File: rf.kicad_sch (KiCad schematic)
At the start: 3 parts, among them J1 ANT_A, J2 ANT_B

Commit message: more stuff
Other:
- moved on the sheet: J1, J2
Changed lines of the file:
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@@
 	)
 	(no_connect
-		(at 196.85 93.98)
+		(at 180.34 93.98)
 	)
 	(wire
 		(pts
-			(xy 175.26 85.09) (xy 196.85 85.09)
+			(xy 175.26 85.09) (xy 180.34 85.09)
 		)
 		(stroke
@@
 		)
 	)
+	(hierarchical_label "TX"
+		(shape output)
+		(at 101.6 95.25 180)
+		(fields_autoplaced yes)
+		(effects
+			(font
+				(size 1.27 1.27)
+			)
+			(justify right)
+		)
+	)
+	(hierarchical_label "DEMOD_OUT"
+		(shape output)
+		(at 101.6 111.76 180)
+		(fields_autoplaced yes)
+		(effects
+			(font
+				(size 1.27 1.27)
+			)
+			(justify right)
+		)
+	)
+	(hierarchical_label "U_BATT"
+		(shape input)
+		(at 101.6 85.09 180)
+		(fields_autoplaced yes)
+		(effects
+			(font
+				(size 1.27 1.27)
+			)
+			(justify right)
+		)
+	)
+	(hierarchical_label "PWR_SEL"
+		(shape input)
+		(at 101.6 102.87 180)
+		(fields_autoplaced yes)
+		(effects
+			(font
+				(size 1.27 1.27)
+			)
+			(justify right)
+		)
+	)
+	(hierarchical_label "ENA"
+		(shape input)
+		(at 101.6 120.65 180)
+		(fields_autoplaced yes)
+		(effects
+			(font
+				(size 1.27 1.27)
+			)
+			(justify right)
+		)
+	)
+	(hierarchical_label "MOD_IN"
+		(shape input)
+		(at 101.6 109.22 180)
+		(fields_autoplaced yes)
+		(effects
+			(font
+				(size 1.27 1.27)
+			)
+			(justify right)
+		)
+	)
+	(hierarchical_label "PTT"
+		(shape input)
+		(at 101.6 116.84 180)
+		(fields_autoplaced yes)
+		(effects
+			(font
+				(size 1.27 1.27)
+			)
+			(justify right)
+		)
+	)
+	(hierarchical_label "RX"
+		(shape input)
+		(at 101.6 97.79 180)
+		(fields_autoplaced yes)
+		(effects
+			(font
+				(size 1.27 1.27)
+			)
+			(justify right)
+		)
+	)
 	(symbol
 		(lib_id "Connector:Conn_01x01_Pin")
-		(at 201.93 85.09 180)
+		(at 185.42 85.09 180)
 		(unit 1)
 		(exclude_from_sim no)
@@
 		(fields_autoplaced yes)
 		(property "Reference" "J1"
-			(at 201.295 80.01 0)
+			(at 184.785 80.01 0)
 			(effects
 				(font
@@
 		)
 		(property "Value" "ANT_A"
-			(at 201.295 82.55 0)
+			(at 184.785 82.55 0)
 			(effects
 				(font
@@
 		)
 		(property "Footprint" "TestPoint:TestPoint_Pad_D2.5mm"
-			(at 201.93 85.09 0)
+			(at 185.42 85.09 0)
 			(effects
 				(font
@@
 		)
 		(property "Datasheet" "~"
-			(at 201.93 85.09 0)
+			(at 185.42 85.09 0)
 			(effects
 				(font
@@
 		)
 		(property "Description" "Generic connector, single row, 01x01, script generated"
-			(at 201.93 85.09 0)
+			(at 185.42 85.09 0)
 			(effects
 				(font
@@
 	(symbol
 		(lib_id "Connector:Conn_01x01_Pin")
-		(at 201.93 93.98 180)
+		(at 185.42 93.98 180)
 		(unit 1)
 		(exclude_from_sim no)
@@
 		(fields_autoplaced yes)
 		(property "Reference" "J2"
-			(at 201.295 88.9 0)
+			(at 184.785 88.9 0)
 			(effects
 				(font
@@
 		)
 		(property "Value" "ANT_B"
-			(at 201.295 91.44 0)
+			(at 184.785 91.44 0)
 			(effects
 				(font
@@
 		)
 		(property "Footprint" "TestPoint:TestPoint_Pad_D2.5mm"
-			(at 201.93 93.98 0)
+			(at 185.42 93.98 0)
 			(effects
 				(font
@@
 		)
 		(property "Datasheet" "~"
-			(at 201.93 93.98 0)
+			(at 185.42 93.98 0)
 			(effects
 				(font
@@
 		)
 		(property "Description" "Generic connector, single row, 01x01, script generated"
-			(at 201.93 93.98 0)
-			(effects
-				(font
+			(at 185.42 93.98 0)
+			(effects
+				(font

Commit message: imported SA868 - thanks, edgetriggered
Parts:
- added U2: SA868, Parts:SA868-VER1.1, symbol Parts:SA868
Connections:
- net DEMOD_OUT: now also U2.3 (AF_OUT)
- net ENA: now also U2.6 (PD)
- net MOD_IN: now also U2.18 (MIC_IN)
- net PTT: now also U2.5 (PTT)
- net PWR_SEL: now also U2.7 (H/L)
- net RX: now also U2.16 (RXD)
- net TX: now also U2.17 (TXD)
- net U_BATT: now also U2.8 (V_{BAT})
- net at FL1.1 (IN): now also U2.12 (ANT)
- net GND: now reaches FL1.2 (GND), FL1.4 (GND)
- net GND: now also U2.10 (GND), U2.9 (GND)
- no-connect marks 1 -> 6
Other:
- note added: "Module programming interface"
- moved on the sheet: FL1, J1, J2

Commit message: connections
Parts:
- renumbered J1 to J2, J2 to J3
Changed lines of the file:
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@@
 	(title_block
 		(title "Mainboard replacement for Nokia 3310")
-		(date "24-10-2024")
+		(date "25-10-2024")
 		(rev "Rev A")
 		(company "M17 Project")
@@
 		(dnp no)
 		(fields_autoplaced yes)
-		(property "Reference" "J1"
+		(property "Reference" "J2"
 			(at 184.785 87.63 0)
 			(effects
@@
 			(project ""
 				(path "/8d65c5ef-7a02-4454-aee5-ab9c49e4aeab/3b860798-5455-4385-a0e7-f7fc9f6a9c55"
-					(reference "J1")
+					(reference "J2")
 					(unit 1)
 				)
@@
 		(dnp no)
 		(fields_autoplaced yes)
-		(property "Reference" "#PWR018"
+		(property "Reference" "#PWR022"
 			(at 165.1 109.22 0)
 			(effects
@@
 			(project ""
 				(path "/8d65c5ef-7a02-4454-aee5-ab9c49e4aeab/3b860798-5455-4385-a0e7-f7fc9f6a9c55"
-					(reference "#PWR018")
+					(reference "#PWR022")
 					(unit 1)
 				)
@@
 		(dnp no)
 		(fields_autoplaced yes)
-		(property "Reference" "J2"
+		(property "Reference" "J3"
 			(at 184.785 96.52 0)
 			(effects
@@
 			(project "M17_3310"
 				(path "/8d65c5ef-7a02-4454-aee5-ab9c49e4aeab/3b860798-5455-4385-a0e7-f7fc9f6a9c55"
-					(reference "J2")
+					(reference "J3")
 					(unit 1)
 				)
@@
 		(dnp no)
 		(fields_autoplaced yes)
-		(property "Reference" "#PWR017"
+		(property "Reference" "#PWR021"
 			(at 121.92 116.84 0)
 			(effects
@@
 			(project "M17_3310"
 				(path "/8d65c5ef-7a02-4454-aee5-ab9c49e4aeab/3b860798-5455-4385-a0e7-f7fc9f6a9c55"
-					(reference "#PWR017")
+					(reference "#PWR021")
 					(unit 1)
 				)

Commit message: audio part
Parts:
- added Q1, Q2: BSS138, Package_TO_SOT_SMD:SOT-23, symbol Transistor_FET:BSS138
- added R7, R8: 100k, Inductor_SMD:L_0805_2012Metric, symbol Device:R
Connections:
- net GND: now also Q1.2 (S), Q2.2 (S), R7.1, R8.1
- net PWR_SEL: now also Q2.1 (G), R8.2; no longer U2.7 (H/L)
- net ENA: no longer names the net of U2.6 (PD)
- net ENA: now also Q1.3 (D)
- new net: Q2.3 (D), U2.7 (H/L)
- new net ~{ENA}: Q1.1 (G), R7.2
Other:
- moved on the sheet: FL1, J2, J3, U2

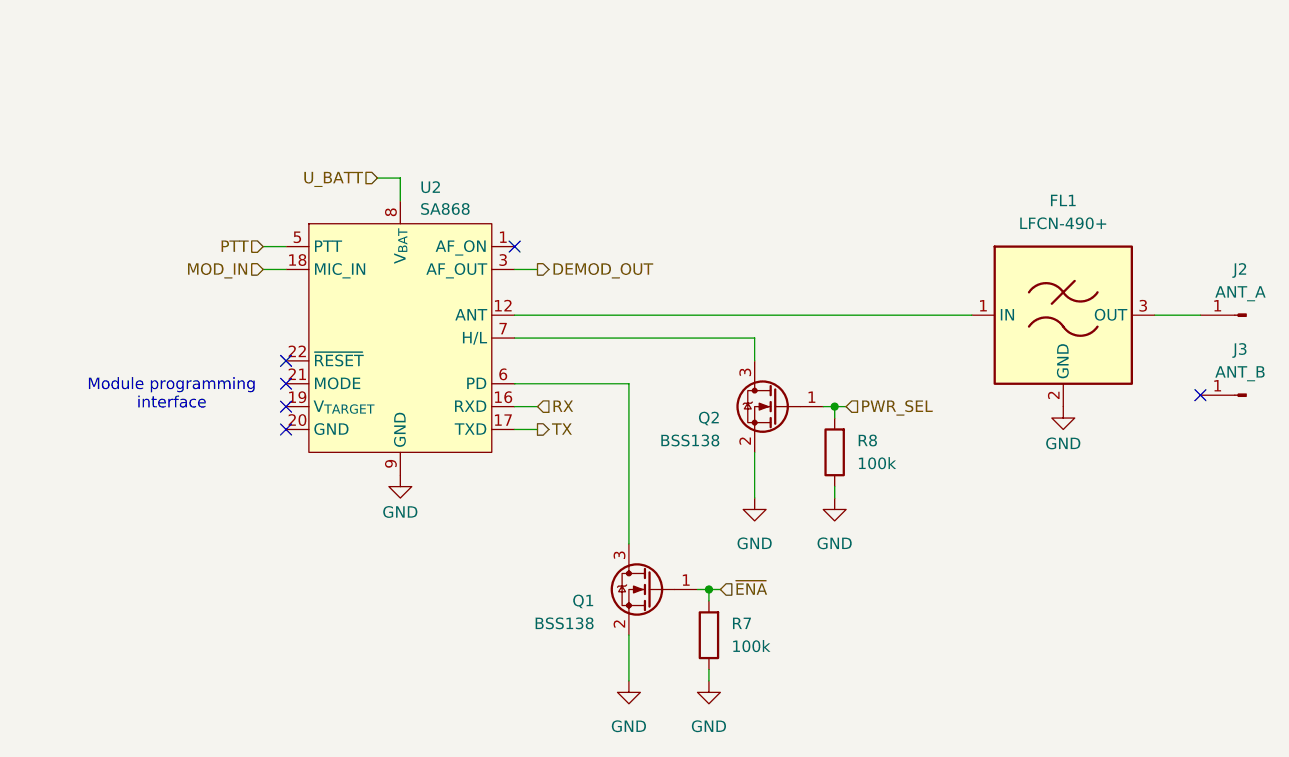
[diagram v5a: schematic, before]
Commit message: spk/mic update
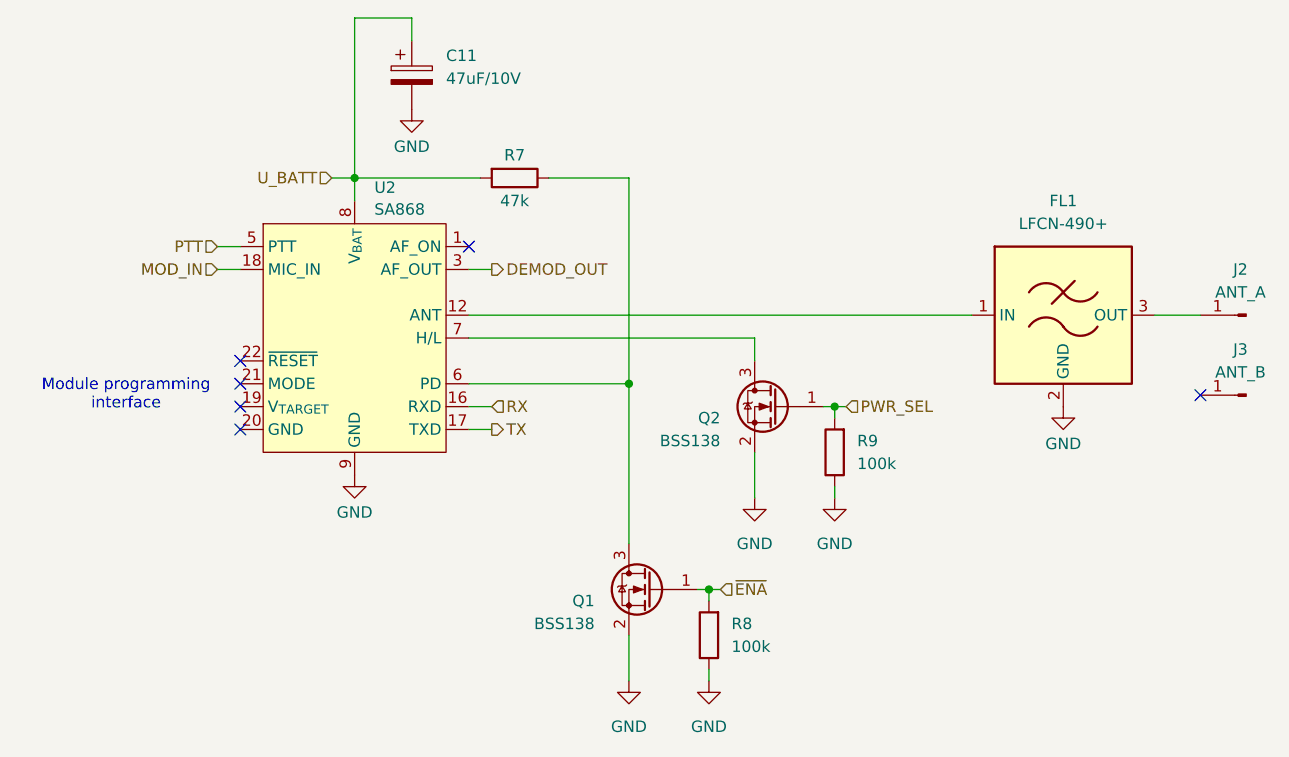
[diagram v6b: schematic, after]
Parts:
- added C11: 47uF/10V, Capacitor_Tantalum_SMD:CP_EIA-3528-21_Kemet-B, symbol Device:C_Polarized
- added R7: 47k, Inductor_SMD:L_0805_2012Metric, symbol Device:R
- renumbered R7 to R8, R8 to R9
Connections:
- net GND: now also C11.2
- net U_BATT: now also C11.1, R7.2
- net at Q1.3 (D), U2.6 (PD): now also R7.1
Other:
- moved on the sheet: U2

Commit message: removed audio part
- added buzzer
- added battery voltage measurement
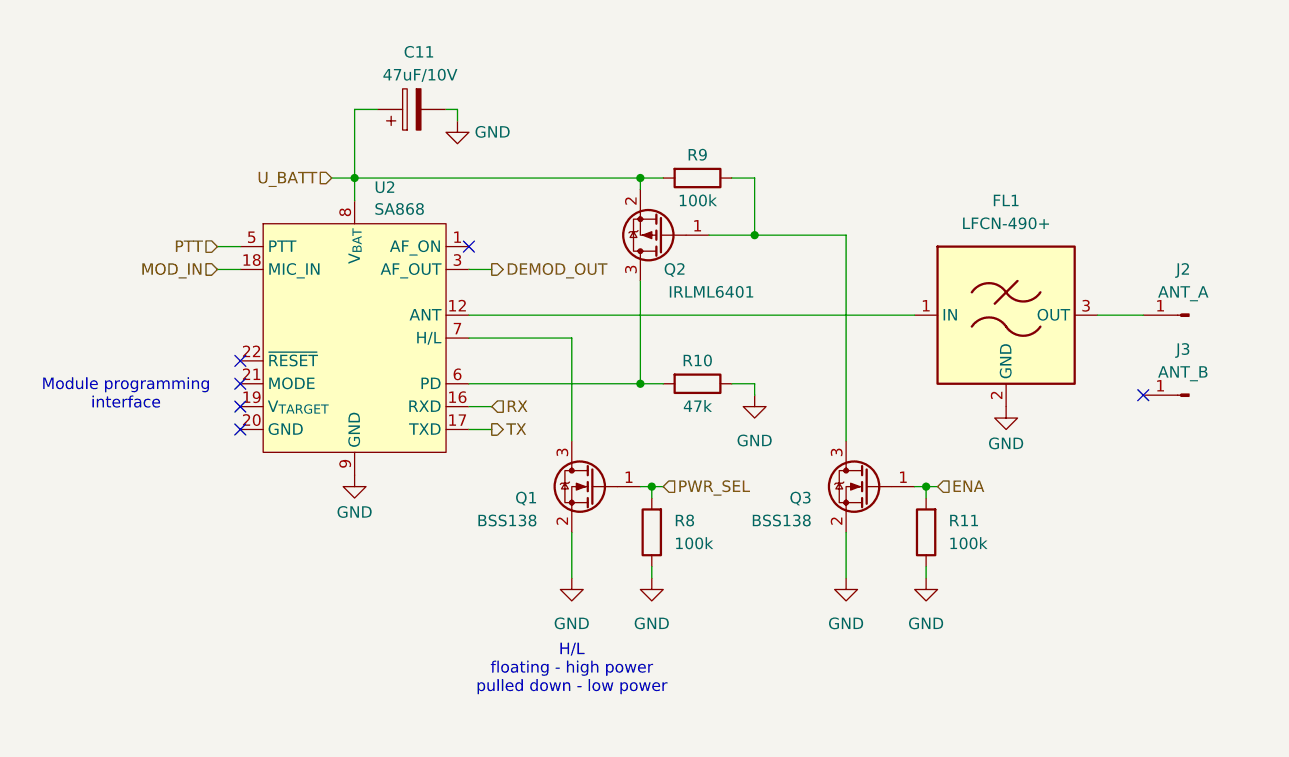
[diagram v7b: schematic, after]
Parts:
- added Q2: IRLML6401, Package_TO_SOT_SMD:SOT-23, symbol Transistor_FET:IRLML6401
- added R10: 47k, Inductor_SMD:L_0805_2012Metric, symbol Device:R
- R9: renamed from R7; value 47k -> 100k
- renumbered Q2 to Q1, Q1 to Q3, R8 to R11, R9 to R8
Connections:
- net GND: now also R10.1
- net U_BATT: now also Q2.2 (S)
- net at Q3.3 (D), R9.1: now also Q2.1 (G); no longer U2.6 (PD)
- net ~{ENA} renamed ENA
- new net: Q2.3 (D), R10.2, U2.6 (PD)
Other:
- note added: "H/L floating - high power pulled down - low power"
- moved on the sheet: C11, FL1, J2, J3, Q1, Q3, R11, R8, R9

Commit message: mayhem
- removed sd card slot
- started pcb design
- added nice 3310 photos
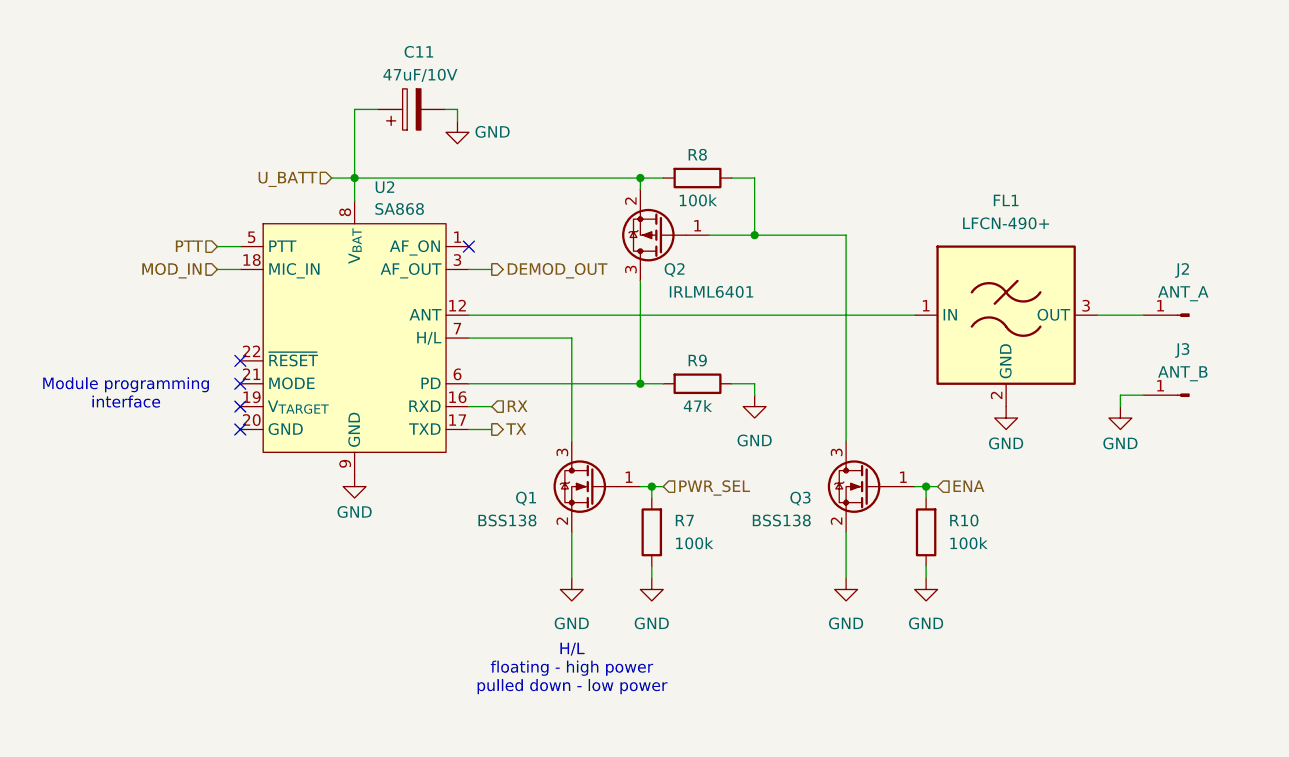
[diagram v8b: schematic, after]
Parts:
- J2, J3: footprint TestPoint:TestPoint_Pad_D2.5mm -> TestPoint:TestPoint_Pad_D1.5mm
- renumbered R11 to R10, R8 to R7, R9 to R8, R10 to R9
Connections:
- net GND: now also J3.1 (Pin_1)
- no-connect marks 6 -> 5
